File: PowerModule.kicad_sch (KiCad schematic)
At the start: 54 parts, among them J8 Conn_02x10_Odd_Even, U20 ADM3485, U21 ADM3485, U22 ADM3485, U23 ADM3485, U24 ADM3485, U25 ADM3485, U26 ADM3485, U66 ADM3485

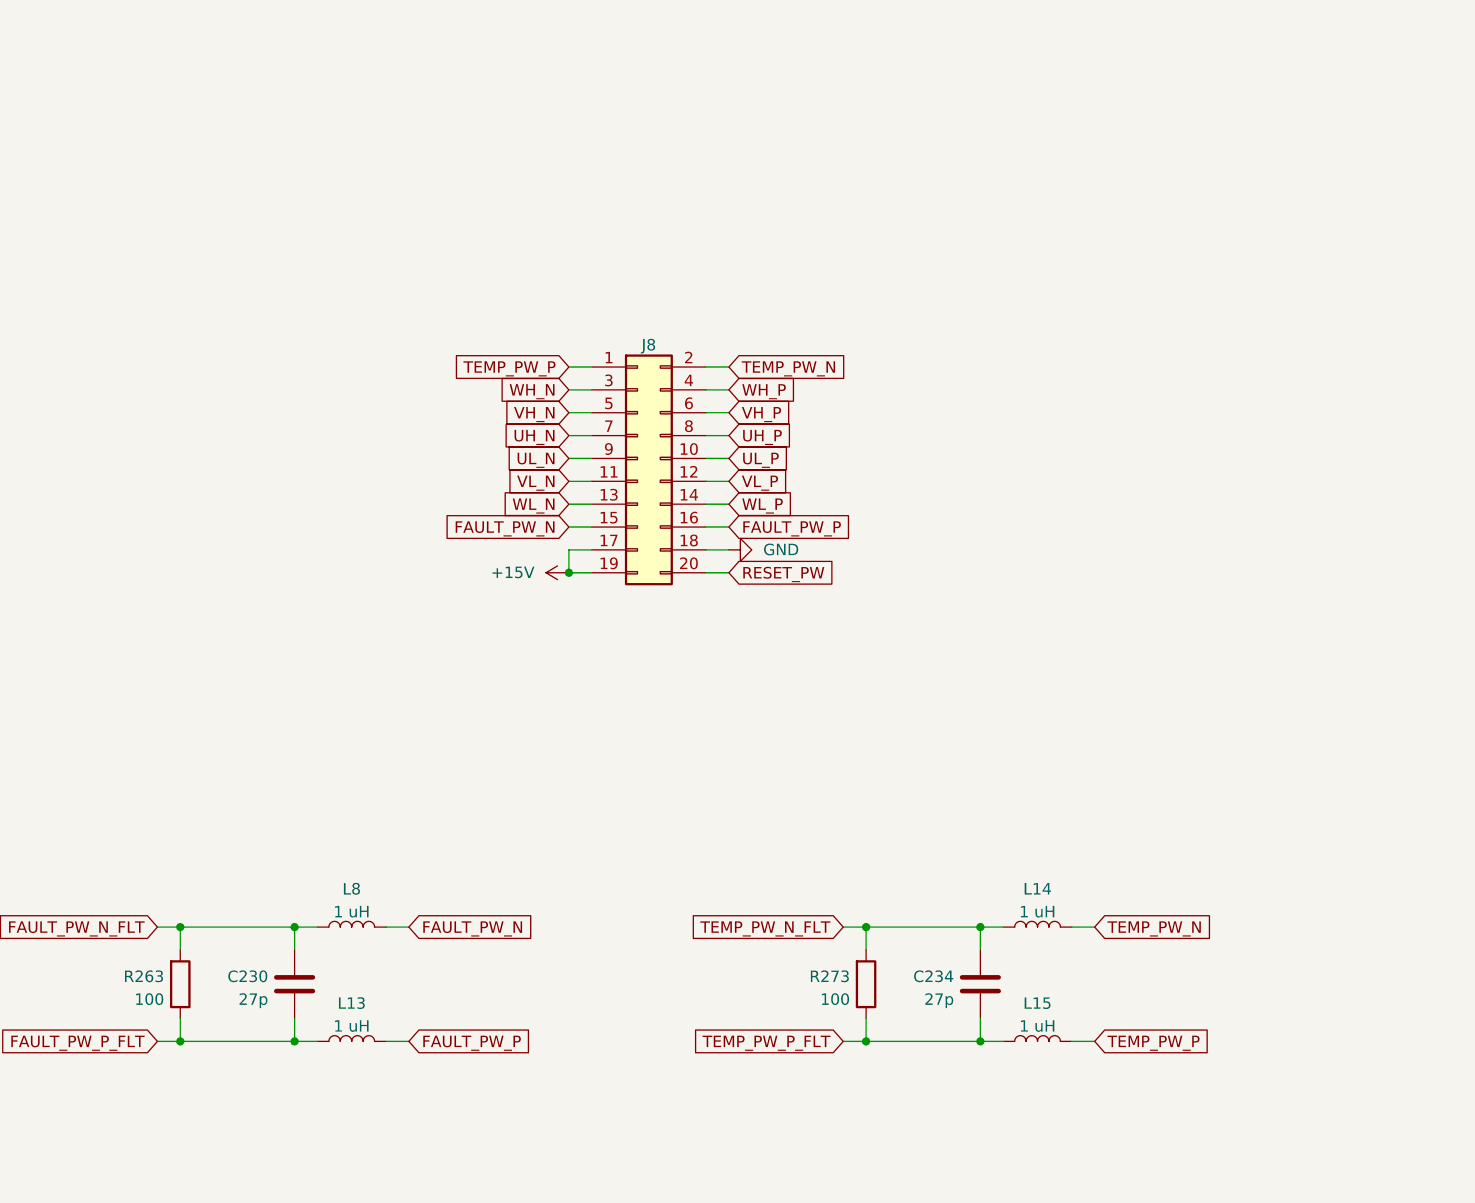
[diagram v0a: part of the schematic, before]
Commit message: Изменения в схеме: убрал разъемы датчиков тока
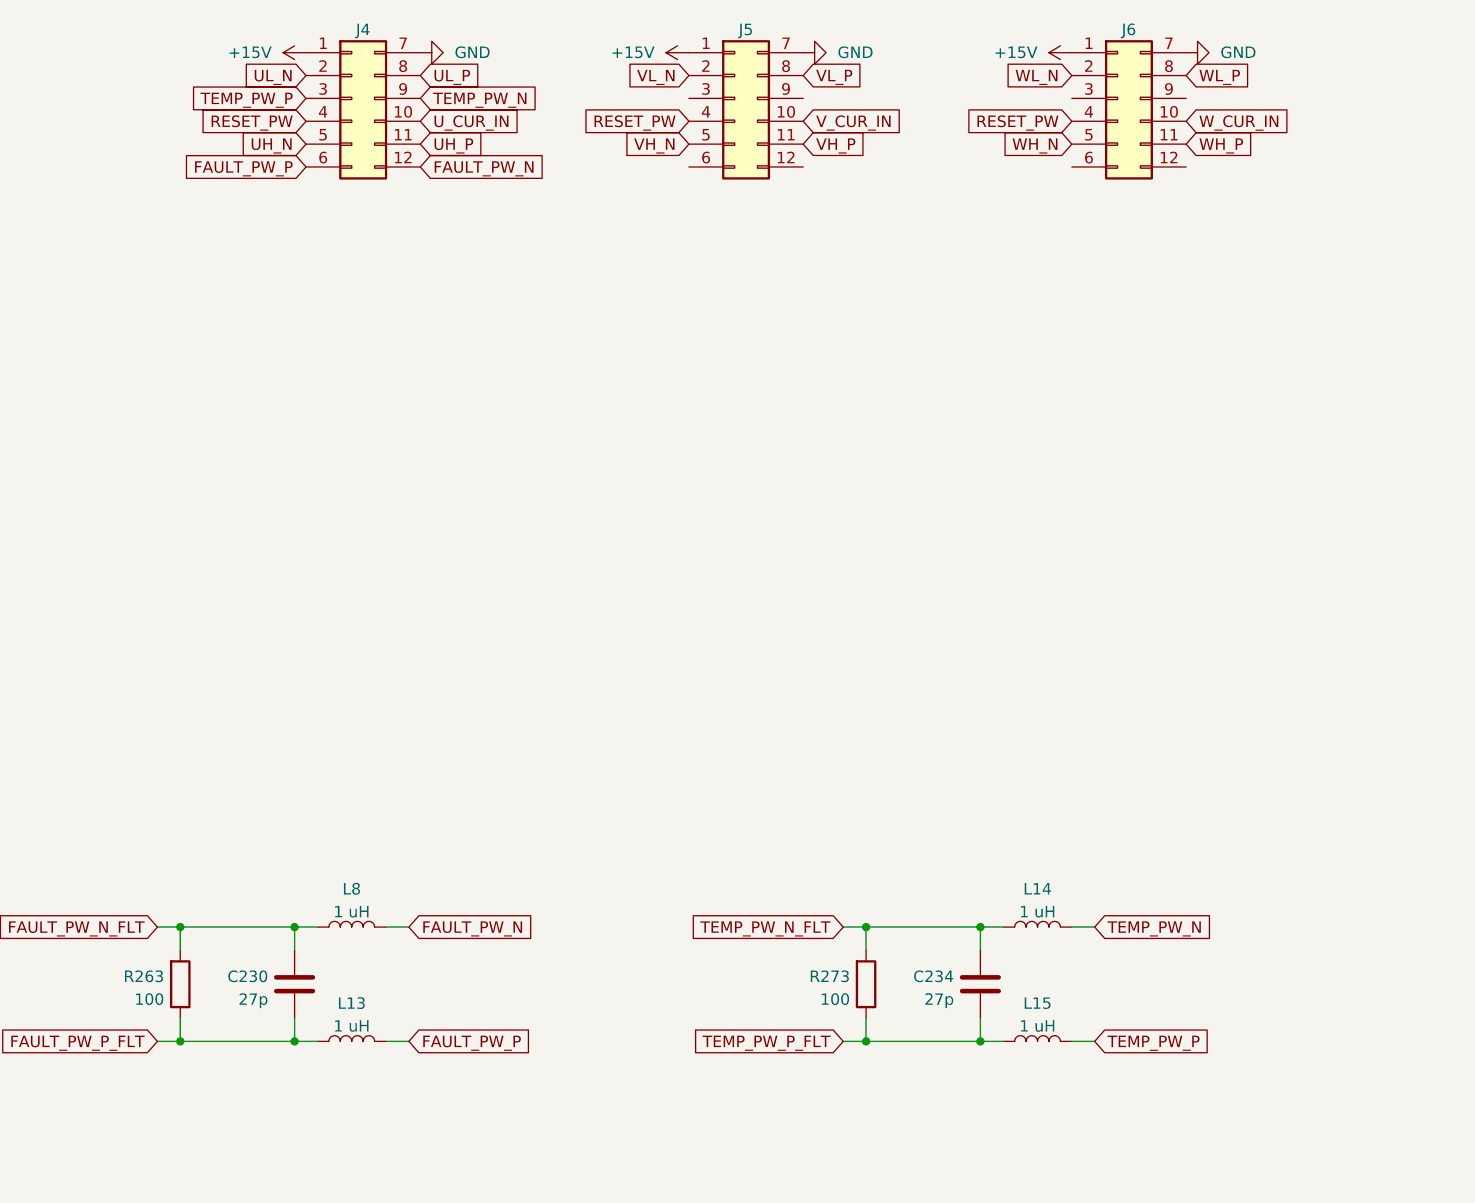
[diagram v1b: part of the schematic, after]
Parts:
- removed J8: Conn_02x10_Odd_Even, Project_Library:2-338069-0, symbol Connector_Generic:Conn_02x10_Odd_Even
- added J4, J5, J6: ~, Connector_Molex:Molex_Micro-Fit_3.0_43045-1200_2x06_P3.00mm_Horizontal, symbol Connector_Generic:Conn_02x06_Top_Bottom
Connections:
- net +15V: now also J4.1 (Pin_1), J5.1 (Pin_1), J6.1 (Pin_1)
- net FAULT_PW_N: now also J4.12 (Pin_12)
- net FAULT_PW_P: now also J4.6 (Pin_6)
- net GND: now also J4.7 (Pin_7), J5.7 (Pin_7), J6.7 (Pin_7)
- net RESET_PW: now also J4.4 (Pin_4), J5.4 (Pin_4), J6.4 (Pin_4)
- net TEMP_PW_N: now also J4.9 (Pin_9)
- net TEMP_PW_P: now also J4.3 (Pin_3)
- net UH_N: now also J4.5 (Pin_5)
- net UH_P: now also J4.11 (Pin_11)
- net UL_N: now also J4.2 (Pin_2)
- net UL_P: now also J4.8 (Pin_8)
- net VH_N: now also J5.5 (Pin_5)
- net VH_P: now also J5.11 (Pin_11)
- net VL_N: now also J5.2 (Pin_2)
- net VL_P: now also J5.8 (Pin_8)
- net WH_N: now also J6.5 (Pin_5)
- net WH_P: now also J6.11 (Pin_11)
- net WL_N: now also J6.2 (Pin_2)
- net WL_P: now also J6.8 (Pin_8)
- new net U_CUR_IN: J4.10 (Pin_10)
- new net V_CUR_IN: J5.10 (Pin_10)
- new net W_CUR_IN: J6.10 (Pin_10)

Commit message: Изменения в схеме: поменял направление меток
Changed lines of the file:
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@@
 	)
 	(global_label "UL_N"
-		(shape input)
+		(shape output)
 		(at 180.34 58.42 0)
 		(fields_autoplaced yes)
@@
 		)
 		(property "Intersheetrefs" "${INTERSHEET_REFS}"
-			(at 187.4098 58.3406 0)
+			(at 187.9819 58.42 0)
 			(effects
 				(font
@@
 	)
 	(global_label "UH_P"
-		(shape input)
+		(shape output)
 		(at 91.44 66.04 0)
 		(fields_autoplaced yes)
@@
 		)
 		(property "Intersheetrefs" "${INTERSHEET_REFS}"
-			(at 98.7517 65.9606 0)
+			(at 99.3238 66.04 0)
 			(effects
 				(font
@@
 	)
 	(global_label "FAULT_PW_N"
-		(shape input)
+		(shape output)
 		(at 285.75 42.545 0)
 		(fields_autoplaced yes)
@@
 	)
 	(global_label "WL_FLT"
-		(shape input)
+		(shape output)
 		(at 332.74 241.3 0)
 		(fields_autoplaced yes)
@@
 		)
 		(property "Intersheetrefs" "${INTERSHEET_REFS}"
-			(at 341.6845 241.2206 0)
+			(at 342.2566 241.3 0)
 			(effects
 				(font
@@
 	)
 	(global_label "WH_N"
-		(shape input)
+		(shape output)
 		(at 91.44 160.02 0)
 		(fields_autoplaced yes)
@@
 		)
 		(property "Intersheetrefs" "${INTERSHEET_REFS}"
-			(at 98.9331 159.9406 0)
+			(at 99.5052 160.02 0)
 			(effects
 				(font
@@
 	)
 	(global_label "VH_FLT"
-		(shape input)
+		(shape output)
 		(at 269.24 203.2 0)
 		(fields_autoplaced yes)
@@
 		)
 		(property "Intersheetrefs" "${INTERSHEET_REFS}"
-			(at 278.1241 203.1206 0)
+			(at 278.6962 203.2 0)
 			(effects
 				(font
@@
 	)
 	(global_label "TEMP_PW_P"
-		(shape input)
+		(shape output)
 		(at 273.05 34.925 180)
 		(fields_autoplaced yes)
@@
 		)
 		(property "Intersheetrefs" "${INTERSHEET_REFS}"
-			(at 259.8721 35.0044 0)
+			(at 259.3002 34.925 0)
 			(effects
 				(font
@@
 	)
 	(global_label "UL_FLT"
-		(shape input)
+		(shape output)
 		(at 332.74 165.1 0)
 		(fields_autoplaced yes)
@@
 		)
 		(property "Intersheetrefs" "${INTERSHEET_REFS}"
-			(at 341.5636 165.0206 0)
+			(at 342.1357 165.1 0)
 			(effects
 				(font
@@
 	)
 	(global_label "RESET_PW"
-		(shape input)
+		(shape passive)
 		(at 373.38 209.55 180)
 		(fields_autoplaced yes)
@@
 		)
 		(property "Intersheetrefs" "${INTERSHEET_REFS}"
-			(at 361.5326 209.6294 0)
+			(at 362.072 209.55 0)
 			(effects
 				(font
@@
 	)
 	(global_label "VH_N"
-		(shape input)
+		(shape output)
 		(at 91.44 109.22 0)
 		(fields_autoplaced yes)
@@
 		)
 		(property "Intersheetrefs" "${INTERSHEET_REFS}"
-			(at 98.5702 109.1406 0)
+			(at 99.1424 109.22 0)
 			(effects
 				(font
@@
 	)
 	(global_label "W_CUR_IN"
-		(shape input)
+		(shape output)
 		(at 370.84 37.465 0)
 		(fields_autoplaced yes)
@@
 		)
 		(property "Intersheetrefs" "${INTERSHEET_REFS}"
-			(at 382.4455 37.3856 0)
+			(at 383.0176 37.465 0)
 			(effects
 				(font
@@
 	)
 	(global_label "VH_P"
-		(shape input)
+		(shape output)
 		(at 91.44 116.84 0)
 		(fields_autoplaced yes)
@@
 		)
 		(property "Intersheetrefs" "${INTERSHEET_REFS}"
-			(at 98.5098 116.7606 0)
+			(at 99.0819 116.84 0)
 			(effects
 				(font
@@
 	)
 	(global_label "VL_P"
-		(shape input)
+		(shape output)
 		(at 180.34 116.84 0)
 		(fields_autoplaced yes)
@@
 		)
 		(property "Intersheetrefs" "${INTERSHEET_REFS}"
-			(at 187.1074 116.7606 0)
+			(at 187.6795 116.84 0)
 			(effects
 				(font
@@
 	)
 	(global_label "FAULT_PW_FLT"
-		(shape input)
+		(shape output)
 		(at 374.65 165.1 180)
 		(fields_autoplaced yes)
@@
 		)
 		(property "Intersheetrefs" "${INTERSHEET_REFS}"
-			(at 358.9926 165.0206 0)
+			(at 358.4205 165.1 0)
 			(effects
 				(font
@@
 	)
 	(global_label "TEMP_PW_P_FLT"
-		(shape input)
+		(shape output)
 		(at 332.74 139.7 180)
 		(fields_autoplaced yes)
@@
 		)
 		(property "Intersheetrefs" "${INTERSHEET_REFS}"
-			(at 315.5102 139.6206 0)
+			(at 314.9383 139.7 0)
 			(effects
 				(font
@@
 	)
 	(global_label "VL_FLT"
-		(shape input)
+		(shape output)
 		(at 332.74 203.2 0)
 		(fields_autoplaced yes)
@@
 		)
 		(property "Intersheetrefs" "${INTERSHEET_REFS}"
-			(at 341.3217 203.1206 0)
+			(at 341.8938 203.2 0)
 			(effects
 				(font
@@
 	)
 	(global_label "TEMP_PW_N_FLT"
-		(shape input)
+		(shape output)
 		(at 332.74 127 180)
 		(fields_autoplaced yes)
@@
 		)
 		(property "Intersheetrefs" "${INTERSHEET_REFS}"
-			(at 315.4498 126.9206 0)
+			(at 314.8778 127 0)
 			(effects
 				(font
@@
 	)
 	(global_label "FAULT_PW_N_FLT"
-		(shape input)
+		(shape output)
 		(at 256.54 127 180)
 		(fields_autoplaced yes)
@@
 		)
 		(property "Intersheetrefs" "${INTERSHEET_REFS}"
-			(at 238.5845 126.9206 0)
+			(at 238.0124 127 0)
 			(effects
 				(font
@@
 	)
 	(global_label "WL_P"
-		(shape input)
+		(shape output)
 		(at 180.34 167.64 0)
 		(fields_autoplaced yes)
@@
 		)
 		(property "Intersheetrefs" "${INTERSHEET_REFS}"
-			(at 187.4702 167.5606 0)
+			(at 188.0423 167.64 0)
 			(effects
 				(font
@@
 	)
 	(global_label "UH_N"
-		(shape input)
+		(shape output)
 		(at 91.44 58.42 0)
 		(fields_autoplaced yes)
@@
 		)
 		(property "Intersheetrefs" "${INTERSHEET_REFS}"
-			(at 98.8121 58.3406 0)
+			(at 99.3843 58.42 0)
 			(effects
 				(font
@@
 	)
 	(global_label "V_CUR_IN"
-		(shape input)
+		(shape output)
 		(at 328.295 37.465 0)
 		(fields_autoplaced yes)
@@
 		)
 		(property "Intersheetrefs" "${INTERSHEET_REFS}"
-			(at 339.5376 37.3856 0)
+			(at 340.1098 37.465 0)
 			(effects
 				(font
@@
 	)
 	(global_label "VL_N"
-		(shape input)
+		(shape output)
 		(at 180.34 109.22 0)
 		(fields_autoplaced yes)
@@
 		)
 		(property "Intersheetrefs" "${INTERSHEET_REFS}"
-			(at 187.1679 109.1406 0)
+			(at 187.74 109.22 0)
 			(effects
 				(font
@@
 	)
 	(global_label "WL_N"
-		(shape input)
+		(shape output)
 		(at 180.34 160.02 0)
 		(fields_autoplaced yes)
@@
 		)
 		(property "Intersheetrefs" "${INTERSHEET_REFS}"
-			(at 187.5307 159.9406 0)
+			(at 188.1028 160.02 0)
 			(effects
 				(font
@@
 	)
 	(global_label "UL_P"
-		(shape input)
+		(shape output)
 		(at 180.34 66.04 0)
 		(fields_autoplaced yes)
@@
 		)
 		(property "Intersheetrefs" "${INTERSHEET_REFS}"
-			(at 187.3493 65.9606 0)
+			(at 187.9214 66.04 0)
 			(effects
 				(font
@@
 	)
 	(global_label "UH_FLT"
-		(shape input)
+		(shape output)
 		(at 269.24 165.1 0)
 		(fields_autoplaced yes)
@@
 		)
 		(property "Intersheetrefs" "${INTERSHEET_REFS}"
-			(at 278.366 165.0206 0)
+			(at 278.9381 165.1 0)
 			(effects
 				(font
@@
 	)
 	(global_label "TEMP_PW_N"
-		(shape input)
+		(shape output)
 		(at 285.75 34.925 0)
 		(fields_autoplaced yes)
@@
 		)
 		(property "Intersheetrefs" "${INTERSHEET_REFS}"
-			(at 298.9883 34.8456 0)
+			(at 299.5603 34.925 0)
 			(effects
 				(font
@@
 	)
 	(global_label "U_CUR_IN"
-		(shape input)
+		(shape output)
 		(at 285.75 37.465 0)
 		(fields_autoplaced yes)
@@
 		)
 		(property "Intersheetrefs" "${INTERSHEET_REFS}"
-			(at 297.2345 37.5444 0)
+			(at 297.8067 37.465 0)
 			(effects
 				(font
@@
 	)
 	(global_label "FAULT_PW_P"
-		(shape input)
+		(shape output)
 		(at 273.05 42.545 180)
 		(fields_autoplaced yes)
@@
 	)
 	(global_label "WH_P"
-		(shape input)
+		(shape output)
 		(at 91.44 167.64 0)
 		(fields_autoplaced yes)
@@
 		)
 		(property "Intersheetrefs" "${INTERSHEET_REFS}"
-			(at 98.8726 167.5606 0)
+			(at 99.4447 167.64 0)
 			(effects
 				(font
@@
 	)
 	(global_label "WH_FLT"
-		(shape input)
+		(shape output)
 		(at 269.24 241.3 0)
 		(fields_autoplaced yes)
@@
 		)
 		(property "Intersheetrefs" "${INTERSHEET_REFS}"
-			(at 278.4869 241.2206 0)
+			(at 279.059 241.3 0)
 			(effects
 				(font
@@
 	)
 	(global_label "FAULT_PW_P_FLT"
-		(shape input)
+		(shape output)
 		(at 256.54 139.7 180)
 		(fields_autoplaced yes)
@@
 		)
 		(property "Intersheetrefs" "${INTERSHEET_REFS}"
-			(at 238.645 139.6206 0)
+			(at 238.0729 139.7 0)
 			(effects
 				(font
@@
 	)
 	(global_label "FAULT_PW"
-		(shape input)
+		(shape output)
 		(at 58.42 223.52 180)
 		(fields_autoplaced yes)
@@
 		)
 		(property "Intersheetrefs" "${INTERSHEET_REFS}"
-			(at 46.8145 223.4406 0)
+			(at 46.2424 223.52 0)
 			(effects
 				(font
@@
 	)
 	(global_label "TEMP_PW_PULSE"
-		(shape input)
+		(shape output)
 		(at 147.32 223.52 180)
 		(fields_autoplaced yes)
@@
 		)
 		(property "Intersheetrefs" "${INTERSHEET_REFS}"
-			(at 129.425 223.4406 0)
-			(effects
-				(font
+			(at 128.8531 223.52 0)
+			(effects
+				(font
